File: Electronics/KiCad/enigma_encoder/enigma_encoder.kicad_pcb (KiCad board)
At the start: 4 copper layers, 81.4 x 76 mm, 25 parts, among them IC1 EPM570T144C5N, J1 Conn_02x20_Odd_Even, J2 Conn_02x20_Odd_Even, J3 Conn_02x06_Odd_Even, J4 Conn_02x05_Odd_Even, Y1 SIT8918BAU71-33E-50.000000G

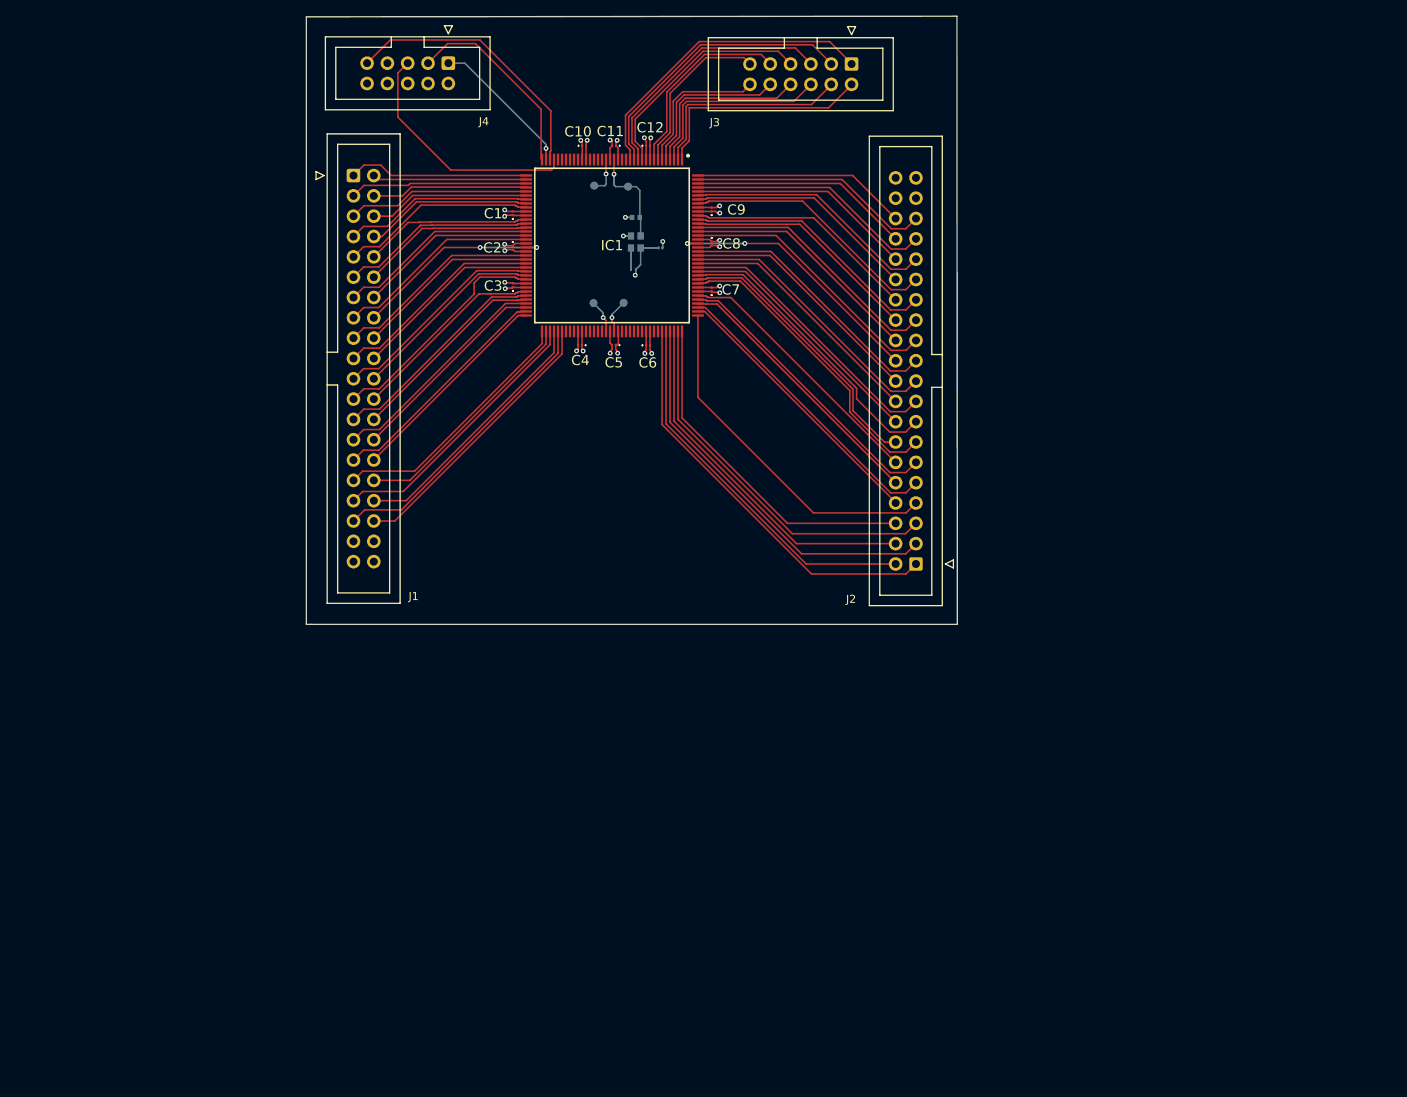
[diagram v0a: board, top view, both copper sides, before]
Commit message: Cleanup of KiCAD area.
General cleanup. Added use of community libraries. Added schematics for encoder, rotor and programmer. Initial design review completed on schematics. Some initial PCB designs created (before schematic changes).
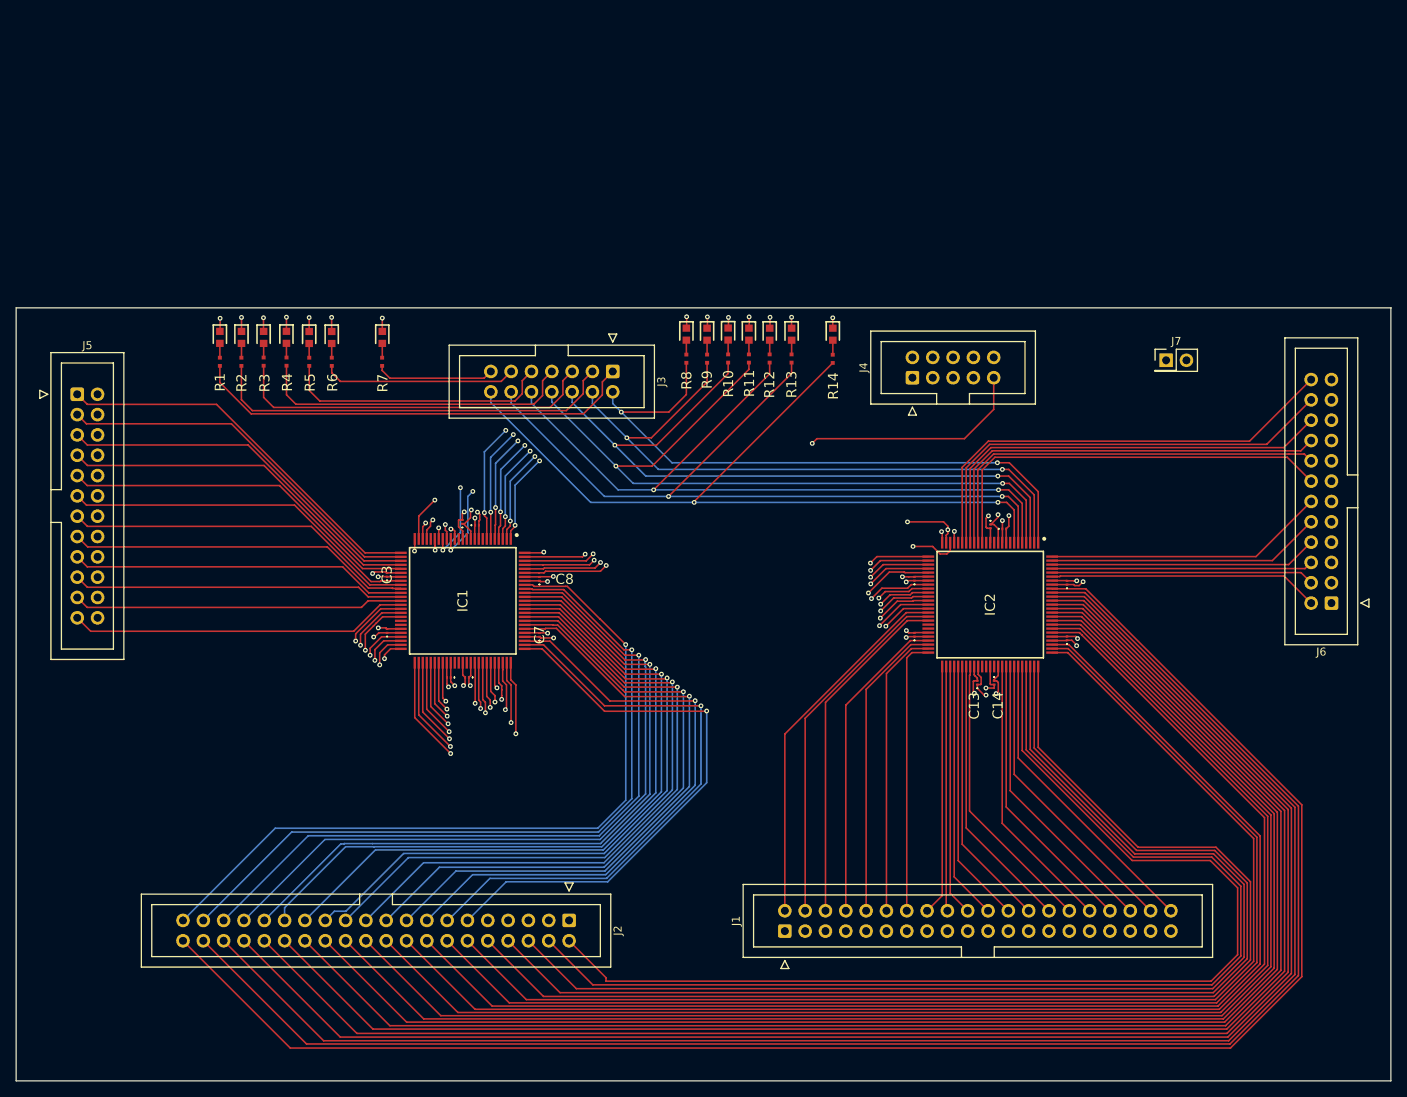
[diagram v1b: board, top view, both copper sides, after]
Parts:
- removed TP1, TP2, TP3, TP4: TestPoint_Small, TestPoint:TestPoint_Pad_D1.0mm
- removed Y1: SIT8918BAU71-33E-50.000000G, SamacSys_Footprints:SIT8918BAU7133E50000000G
- added C15: GRM033Z71A104ME14D, Enigma_Components:GRM033D70J224ME01D, F.Cu at (208.8, 91.3)
- added C16: GRM033Z71A104ME14D, Enigma_Components:GRM033D70J224ME01D, F.Cu at (208.8, 84.3)
- added IC2: EPM240T100C5N, Enigma_Components:QFP50P1600X1600X120-100N, F.Cu at (199.2, 87.1)
- added J5: Conn_02x12_Odd_Even, Connector_IDC:IDC-Header_2x12_P2.54mm_Vertical, F.Cu at (85.1, 60.8)
- added J6: Conn_02x12_Odd_Even, Connector_IDC:IDC-Header_2x12_P2.54mm_Vertical, F.Cu at (241.9, 86.9)
- added J7: Conn_02x01, Connector_PinHeader_2.54mm:PinHeader_2x01_P2.54mm_Vertical, F.Cu at (221.2, 56.5)
- added LED1: KT-0603R, Enigma_Components:LEDC1608X70N, F.Cu at (103.0, 53.7)
- added LED10: KT-0603R, Enigma_Components:LEDC1608X70N, F.Cu at (166.5, 53.3)
- added LED11: KT-0603R, Enigma_Components:LEDC1608X70N, F.Cu at (169.1, 53.3)
- added LED12: KT-0603R, Enigma_Components:LEDC1608X70N, F.Cu at (171.7, 53.3)
- added LED13: KT-0603R, Enigma_Components:LEDC1608X70N, F.Cu at (174.4, 53.3)
- added LED14: KT-0603R, Enigma_Components:LEDC1608X70N, F.Cu at (179.6, 53.3)
- added LED2: KT-0603R, Enigma_Components:LEDC1608X70N, F.Cu at (105.7, 53.7)
- added LED3: KT-0603R, Enigma_Components:LEDC1608X70N, F.Cu at (108.4, 53.7)
- added LED4: KT-0603R, Enigma_Components:LEDC1608X70N, F.Cu at (111.3, 53.7)
- added LED5: KT-0603R, Enigma_Components:LEDC1608X70N, F.Cu at (114.1, 53.7)
- added LED6: KT-0603R, Enigma_Components:LEDC1608X70N, F.Cu at (116.9, 53.7)
- added LED7: KT-0603R, Enigma_Components:LEDC1608X70N, F.Cu at (123.2, 53.7)
- added LED8: KT-0603R, Enigma_Components:LEDC1608X70N, F.Cu at (161.3, 53.3)
- added LED9: KT-0603R, Enigma_Components:LEDC1608X70N, F.Cu at (163.8, 53.3)
- added R10: ERA2AEB201X, Enigma_Components:ERA2AED122X, F.Cu at (166.5, 56.3)
- added R11: ERA2AEB201X, Enigma_Components:ERA2AED122X, F.Cu at (169.1, 56.3)
- added R12: ERA2AEB201X, Enigma_Components:ERA2AED122X, F.Cu at (171.7, 56.3)
- added R13: ERA2AEB201X, Enigma_Components:ERA2AED122X, F.Cu at (174.4, 56.3)
- added R14: ERA2AEB201X, Enigma_Components:ERA2AED122X, F.Cu at (179.6, 56.4)
- added R2: ERA2AEB201X, Enigma_Components:ERA2AED122X, F.Cu at (105.6, 56.7)
- added R3: ERA2AEB201X, Enigma_Components:ERA2AED122X, F.Cu at (108.4, 56.7)
- added R4: ERA2AEB201X, Enigma_Components:ERA2AED122X, F.Cu at (111.3, 56.7)
- added R5: ERA2AEB201X, Enigma_Components:ERA2AED122X, F.Cu at (114.1, 56.7)
- added R6: ERA2AEB201X, Enigma_Components:ERA2AED122X, F.Cu at (116.9, 56.7)
- added R7: ERA2AEB201X, Enigma_Components:ERA2AED122X, F.Cu at (123.2, 56.7)
- added R8: ERA2AEB201X, Enigma_Components:ERA2AED122X, F.Cu at (161.3, 56.4)
- added R9: ERA2AEB201X, Enigma_Components:ERA2AED122X, F.Cu at (163.8, 56.4)
- C1, C10, C11, C12, C2, C3, C4, C5, C6, C7, C8, C9: footprint SamacSys_Footprints:GRM033D70J224ME01D -> Enigma_Components:GRM033D70J224ME01D
- C13: footprint SamacSys_Footprints:GRM033D70J224ME01D -> Enigma_Components:GRM033D70J224ME01D; moved to F.Cu
- C14: value VJ0402A150FXQCW1BC -> GRM033Z71A104ME14D; footprint SamacSys_Footprints:CAPC1005X55N -> Enigma_Components:GRM033D70J224ME01D; moved to F.Cu
- IC1: value EPM570T144C5N -> EPM240T100C5N; footprint SamacSys_Footprints:QFP50P2200X2200X160-144N -> Enigma_Components:QFP50P1600X1600X120-100N
- J3: value Conn_02x06_Odd_Even -> Conn_02x07_Odd_Even; footprint Connector_IDC:IDC-Header_2x06_P2.54mm_Vertical -> Connector_IDC:IDC-Header_2x07_P2.54mm_Vertical
- R1: value ERJ-1GNF1001C -> ERA2AEB201X; footprint SamacSys_Footprints:ERJ1GN__0201_ -> Enigma_Components:ERA2AED122X; moved to F.Cu
- moved J1 108.7 mm to (173.6, 127.9), turned to 90 degrees
- moved C14 73.4 mm to (199.7, 96.8), turned to -90 degrees
- moved J4 70.1 mm to (189.5, 58.7), turned to 90 degrees
- moved C12 69.6 mm to (189.8, 90.9), turned to 90 degrees
- moved C10 69.6 mm to (199.3, 77.3), turned to -90 degrees
- moved C13 67.2 mm to (197.6, 96.8), turned to 90 degrees
- moved C11 65.9 mm to (189.8, 83.9), turned to 90 degrees
- moved J2 62.2 mm to (146.6, 126.6), turned to -90 degrees
- moved C9 54.1 mm to (201.0, 77.6), turned to 0 degrees
- moved R1 53.0 mm to (103.0, 56.7), turned to -90 degrees
- moved J3 48.7 mm to (152.1, 58.0)
- moved C7 48.2 mm to (142.9, 90.9)
- moved IC1 48.2 mm to (133.3, 86.6)
- moved C6 47.3 mm to (133.8, 96.2), turned to 180 degrees
- moved C8 47.1 mm to (142.9, 83.9), turned to 90 degrees
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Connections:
- C14 pad 2: /LCLK1 -> VCC
- IC1 pad 1: /BIN_OUT_01 -> /BIN_IN_01
- IC1 pad 100: VCC -> /KEY_OUT_58
- IC1 pad 11: /BIN_IN_04 -> GND
- IC1 pad 12: /BIN_IN_03 -> unconnected-(IC1-IO/GCLK0-Pad12)
- IC1 pad 13: /BIN_IN_02 -> VCC
- IC1 pad 14: /BIN_IN_01 -> unconnected-(IC1-IO/GCLK1-Pad14)
- IC1 pad 15: unconnected-(IC1-IO_13-Pad15) -> /KEY_OUT_59
- IC1 pad 16: unconnected-(IC1-IO_14-Pad16) -> /KEY_OUT_60
- IC1 pad 17: GND -> /KEY_OUT_61
- IC1 pad 18: /LCLK1 -> /KEY_OUT_62
- IC1 pad 19: VCC -> /KEY_OUT_63
- IC1 pad 2: /BIN_OUT_02 -> /BIN_IN_02
- IC1 pad 20: /LCLK2 -> /KEY_OUT_64
- IC1 pad 22: unconnected-(IC1-IO_16-Pad22) -> /JTAG_TMS
- IC1 pad 23: unconnected-(IC1-IO_17-Pad23) -> /JTAG_TDI
- IC1 pad 24: unconnected-(IC1-IO_18-Pad24) -> /JTAG_TCK
- IC1 pad 25: VCC -> /JTAG_TDX
- IC1 pad 26: GND -> /KEY_OUT_01
- IC1 pad 27: unconnected-(IC1-IO_19-Pad27) -> /KEY_OUT_02
- IC1 pad 28: unconnected-(IC1-IO_20-Pad28) -> /KEY_OUT_03
- IC1 pad 29: unconnected-(IC1-IO_21-Pad29) -> /KEY_OUT_04
- IC1 pad 3: /BIN_OUT_03 -> /BIN_IN_03
- IC1 pad 30: unconnected-(IC1-IO_22-Pad30) -> /KEY_OUT_05
- IC1 pad 31: unconnected-(IC1-IO_23-Pad31) -> VCC
- IC1 pad 32: unconnected-(IC1-IO_24-Pad32) -> GND
- IC1 pad 33: /JTAG_TMS -> /KEY_OUT_06
- IC1 pad 34: /JTAG_TDI -> /KEY_OUT_07
- IC1 pad 35: /JTAG_TCK -> /KEY_OUT_08
- IC1 pad 36: /JTAG_TDO -> /KEY_OUT_09
- IC1 pad 37: /KEY_IN_01 -> /KEY_OUT_10
- IC1 pad 38: /KEY_OUT_01 -> /KEY_OUT_11
- IC1 pad 39: /KEY_IN_02 -> /KEY_OUT_12
- IC1 pad 4: /BIN_OUT_04 -> /BIN_IN_04
- IC1 pad 40: /KEY_OUT_02 -> /KEY_OUT_13
- IC1 pad 41: /KEY_IN_03 -> /KEY_OUT_14
- IC1 pad 42: /KEY_OUT_03 -> /KEY_OUT_15
- IC1 pad 43: /KEY_IN_04 -> unconnected-(IC1-IO/DEV_OE-Pad43)
- IC1 pad 44: /KEY_OUT_04 -> unconnected-(IC1-IO/DEV_CLRN-Pad44)
- IC1 pad 45: /KEY_IN_05 -> VCC
- IC1 pad 46: VCC -> GND
- IC1 pad 47: GND -> /KEY_OUT_16
- IC1 pad 48: /KEY_OUT_05 -> /KEY_OUT_17
- IC1 pad 49: /KEY_IN_06 -> /KEY_OUT_18
- IC1 pad 5: /BIN_OUT_05 -> /BIN_IN_05
- IC1 pad 50: /KEY_OUT_06 -> /KEY_OUT_19
- IC1 pad 51: /KEY_IN_07 -> /KEY_OUT_20
- IC1 pad 52: /KEY_OUT_07 -> /KEY_OUT_21
- IC1 pad 53: /KEY_IN_08 -> /KEY_OUT_22
- IC1 pad 54: GND -> /KEY_OUT_23
- IC1 pad 55: /KEY_OUT_08 -> /KEY_OUT_24
- IC1 pad 56: VCC -> /KEY_OUT_25
- IC1 pad 57: /KEY_IN_09 -> /KEY_OUT_26
- IC1 pad 58: /KEY_OUT_09 -> /KEY_OUT_27
- IC1 pad 59: /KEY_IN_10 -> VCC
- IC1 pad 6: /BIN_OUT_06 -> /BIN_IN_06
- IC1 pad 60: /KEY_OUT_10 -> GND
- IC1 pad 61: /KEY_IN_11 -> unconnected-(IC1-IO_43-Pad61)
- IC1 pad 62: /KEY_OUT_11 -> unconnected-(IC1-IO/GCLK2-Pad62)
- IC1 pad 63: /KEY_IN_12 -> VCC
- IC1 pad 64: VCC -> unconnected-(IC1-IO/GCLK3-Pad64)
- IC1 pad 66: /KEY_OUT_12 -> /KEY_OUT_28
- IC1 pad 67: /KEY_IN_13 -> /KEY_OUT_29
- IC1 pad 68: /KEY_OUT_13 -> /KEY_OUT_30
- IC1 pad 69: /KEY_IN_14 -> /KEY_OUT_31
- IC1 pad 7: /BIN_IN_06 -> /BIN_IN_EN
- IC1 pad 70: /KEY_OUT_14 -> /KEY_OUT_32
- IC1 pad 71: /KEY_IN_15 -> /KEY_OUT_33
- IC1 pad 72: /KEY_OUT_15 -> /KEY_OUT_34
- IC1 pad 73: /KEY_IN_16 -> /KEY_OUT_35
- IC1 pad 74: /KEY_OUT_16 -> /KEY_OUT_36
- IC1 pad 75: /KEY_IN_17 -> /KEY_OUT_37
- IC1 pad 76: /KEY_OUT_17 -> /KEY_OUT_38
- IC1 pad 77: /KEY_IN_18 -> /KEY_OUT_39
- IC1 pad 78: /KEY_OUT_18 -> /KEY_OUT_40
- IC1 pad 79: unconnected-(IC1-IO_59-Pad79) -> GND
- IC1 pad 8: /BIN_IN_05 -> unconnected-(IC1-IO_8-Pad8)
- IC1 pad 80: unconnected-(IC1-IO_60-Pad80) -> VCC
- IC1 pad 81: unconnected-(IC1-IO_61-Pad81) -> /KEY_OUT_41
- IC1 pad 82: VCC -> /KEY_OUT_42
- IC1 pad 83: GND -> /KEY_OUT_43
- IC1 pad 84: unconnected-(IC1-IO_62-Pad84) -> /KEY_OUT_44
- IC1 pad 85: unconnected-(IC1-IO_63-Pad85) -> /KEY_OUT_45
- IC1 pad 86: unconnected-(IC1-IO_64-Pad86) -> /KEY_OUT_46
- IC1 pad 87: unconnected-(IC1-IO_65-Pad87) -> /KEY_OUT_47
- IC1 pad 88: unconnected-(IC1-IO_66-Pad88) -> /KEY_OUT_48
- IC1 pad 89: /LCLK4 -> /KEY_OUT_49
- IC1 pad 90: VCC -> /KEY_OUT_50
- IC1 pad 91: /LCLK3 -> /KEY_OUT_51
- IC1 pad 92: GND -> /KEY_OUT_52
- IC1 pad 93: unconnected-(IC1-IO_67-Pad93) -> GND
- IC1 pad 94: unconnected-(IC1-IO_68-Pad94) -> VCC
- IC1 pad 95: unconnected-(IC1-IO_69-Pad95) -> /KEY_OUT_53
- IC1 pad 96: unconnected-(IC1-IO_70-Pad96) -> /KEY_OUT_54
- IC1 pad 97: unconnected-(IC1-IO_71-Pad97) -> /KEY_OUT_55
- IC1 pad 98: unconnected-(IC1-IO_72-Pad98) -> /KEY_OUT_56
- IC1 pad 99: GND -> /KEY_OUT_57
- J1 pad 1: /KEY_IN_01 -> /KEY_OUT_13
- J1 pad 10: /KEY_OUT_05 -> /KEY_IN_17
- J1 pad 11: /KEY_IN_06 -> /KEY_OUT_18
- J1 pad 12: /KEY_OUT_06 -> /KEY_IN_18
- J1 pad 13: /KEY_IN_07 -> /KEY_OUT_19
- J1 pad 14: /KEY_OUT_07 -> /KEY_IN_19
- J1 pad 15: /KEY_IN_08 -> /KEY_OUT_20
- J1 pad 16: /KEY_OUT_08 -> /KEY_IN_20
- J1 pad 17: /KEY_IN_09 -> /KEY_OUT_21
- J1 pad 18: /KEY_OUT_09 -> /KEY_IN_21
- J1 pad 19: /KEY_IN_10 -> /KEY_OUT_22
- J1 pad 2: /KEY_OUT_01 -> /KEY_IN_13
- J1 pad 20: /KEY_OUT_10 -> /KEY_IN_22
- J1 pad 21: /KEY_IN_11 -> /KEY_OUT_23
- J1 pad 22: /KEY_OUT_11 -> /KEY_IN_23
- J1 pad 23: /KEY_IN_12 -> /KEY_OUT_24
- J1 pad 24: /KEY_OUT_12 -> /KEY_IN_24
- J1 pad 25: /KEY_IN_13 -> /KEY_OUT_25
- J1 pad 26: /KEY_OUT_13 -> /KEY_IN_25
- J1 pad 27: /KEY_IN_14 -> /KEY_OUT_26
- J1 pad 28: /KEY_OUT_14 -> /KEY_IN_26
- J1 pad 29: /KEY_IN_15 -> /KEY_OUT_27
- J1 pad 3: /KEY_IN_02 -> /KEY_OUT_14
- J1 pad 30: /KEY_OUT_15 -> /KEY_IN_27
- J1 pad 31: /KEY_IN_16 -> /KEY_OUT_28
- J1 pad 32: /KEY_OUT_16 -> /KEY_IN_28
- J1 pad 33: /KEY_IN_17 -> /KEY_OUT_29
- J1 pad 34: /KEY_OUT_17 -> /KEY_IN_29
- J1 pad 35: /KEY_IN_18 -> /KEY_OUT_30
- J1 pad 36: /KEY_OUT_18 -> /KEY_IN_30
- J1 pad 37: unconnected-(J1-Pin_37-Pad37) -> /KEY_OUT_31
- J1 pad 38: unconnected-(J1-Pin_38-Pad38) -> /KEY_IN_31
- J1 pad 39: unconnected-(J1-Pin_39-Pad39) -> /KEY_OUT_32
- J1 pad 4: /KEY_OUT_02 -> /KEY_IN_14
- J1 pad 40: unconnected-(J1-Pin_40-Pad40) -> /KEY_IN_32
- J1 pad 5: /KEY_IN_03 -> /KEY_OUT_15
- J1 pad 6: /KEY_OUT_03 -> /KEY_IN_15
- J1 pad 7: /KEY_IN_04 -> /KEY_OUT_16
- J1 pad 8: /KEY_OUT_04 -> /KEY_IN_16
- J1 pad 9: /KEY_IN_05 -> /KEY_OUT_17
- J2 pad 1: /KEY_IN_19 -> /KEY_OUT_33
- J2 pad 10: /KEY_OUT_23 -> /KEY_IN_37
- J2 pad 11: /KEY_IN_24 -> /KEY_OUT_38
- J2 pad 12: /KEY_OUT_24 -> /KEY_IN_38
- J2 pad 13: /KEY_IN_25 -> /KEY_OUT_39
- J2 pad 14: /KEY_OUT_25 -> /KEY_IN_39
- J2 pad 15: /KEY_IN_26 -> /KEY_OUT_40
- J2 pad 16: /KEY_OUT_26 -> /KEY_IN_40
- J2 pad 17: /KEY_IN_27 -> /KEY_OUT_41
- J2 pad 18: /KEY_OUT_27 -> /KEY_IN_41
- J2 pad 19: /KEY_IN_28 -> /KEY_OUT_42
- J2 pad 2: /KEY_OUT_19 -> /KEY_IN_33
- J2 pad 20: /KEY_OUT_28 -> /KEY_IN_42
- J2 pad 21: /KEY_IN_29 -> /KEY_OUT_43
- J2 pad 22: /KEY_OUT_29 -> /KEY_IN_43
- J2 pad 23: /KEY_IN_30 -> /KEY_OUT_44
- J2 pad 24: /KEY_OUT_30 -> /KEY_IN_44
- J2 pad 25: /KEY_IN_31 -> /KEY_OUT_45
- J2 pad 26: /KEY_OUT_31 -> /KEY_IN_45
- J2 pad 27: /KEY_IN_32 -> /KEY_OUT_46
- J2 pad 28: /KEY_OUT_32 -> /KEY_IN_46
- J2 pad 29: /KEY_IN_33 -> /KEY_OUT_47
- J2 pad 3: /KEY_IN_20 -> /KEY_OUT_34
- J2 pad 30: /KEY_OUT_33 -> /KEY_IN_47
- J2 pad 31: /KEY_IN_34 -> /KEY_OUT_48
- J2 pad 32: /KEY_OUT_34 -> /KEY_IN_48
- J2 pad 33: /KEY_IN_35 -> /KEY_OUT_49
- J2 pad 34: /KEY_OUT_35 -> /KEY_IN_49
- J2 pad 35: /KEY_IN_36 -> /KEY_OUT_50
- J2 pad 36: /KEY_OUT_36 -> /KEY_IN_50
- J2 pad 37: unconnected-(J2-Pin_37-Pad37) -> /KEY_OUT_51
- J2 pad 38: unconnected-(J2-Pin_38-Pad38) -> /KEY_IN_51
- J2 pad 39: unconnected-(J2-Pin_39-Pad39) -> /KEY_OUT_52
- J2 pad 4: /KEY_OUT_20 -> /KEY_IN_34
- J2 pad 40: unconnected-(J2-Pin_40-Pad40) -> /KEY_IN_52
- J2 pad 5: /KEY_IN_21 -> /KEY_OUT_35
- J2 pad 6: /KEY_OUT_21 -> /KEY_IN_35
- J2 pad 7: /KEY_IN_22 -> /KEY_OUT_36
- J2 pad 8: /KEY_OUT_22 -> /KEY_IN_36
- J2 pad 9: /KEY_IN_23 -> /KEY_OUT_37
- R1 pad 1: VCC -> Net-(LED1-Pad2)
- R1 pad 2: Net-(Y1-OE) -> /BIN_IN_01
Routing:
- net /KEY_IN_52: track 0.00 -> 213.0 mm
- net /KEY_IN_51: track 0.00 -> 208.8 mm
- net /KEY_IN_50: track 0.00 -> 204.7 mm
- net /KEY_IN_49: track 0.00 -> 200.5 mm
- net /KEY_IN_48: track 0.00 -> 196.4 mm
- net /KEY_IN_47: track 0.00 -> 192.2 mm
- net /KEY_IN_46: track 0.00 -> 188.0 mm
- net /KEY_IN_45: track 0.00 -> 183.9 mm
- net /KEY_IN_44: track 0.00 -> 179.8 mm
- net /KEY_IN_43: track 0.00 -> 175.7 mm
- net /KEY_IN_42: track 0.00 -> 171.7 mm
- net /KEY_IN_41: track 0.00 -> 167.6 mm
- net /KEY_IN_40: track 0.00 -> 161.6 mm
- net /KEY_IN_39: track 0.00 -> 157.6 mm
- net /KEY_IN_37: track 0.00 -> 153.5 mm
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- added copper zone on In3.Cu, net VCC
- removed copper zone on In2.Cu, net VCC
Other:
- board size 81.4 x 76 mm -> 171.8 x 96.6 mm
- copper layers 4 -> 6
- board text removed: "C6"
